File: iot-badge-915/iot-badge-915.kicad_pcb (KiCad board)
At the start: 2 copper layers, 70 x 100 mm, 68 parts, among them J1 USB_C_Receptacle_USB2.0, J2 Wire ANT, J3 Conn_01x04_Male, Q1 BC847, Q2 BC847, Q3 BC847, SW1 SW_Push, SW2 SW_Push, SW3 SW_Push, SW4 SW_Push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

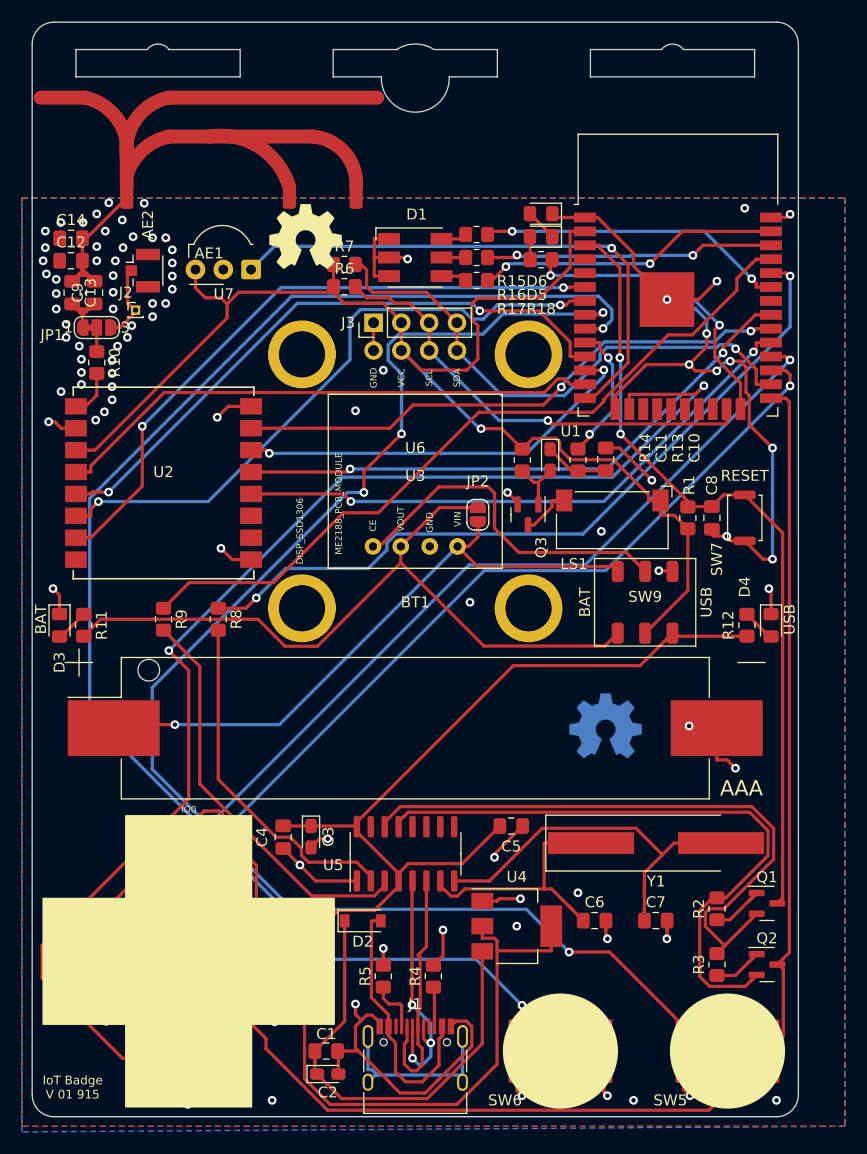
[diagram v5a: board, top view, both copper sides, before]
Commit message: added and routed audio components in 915mhz
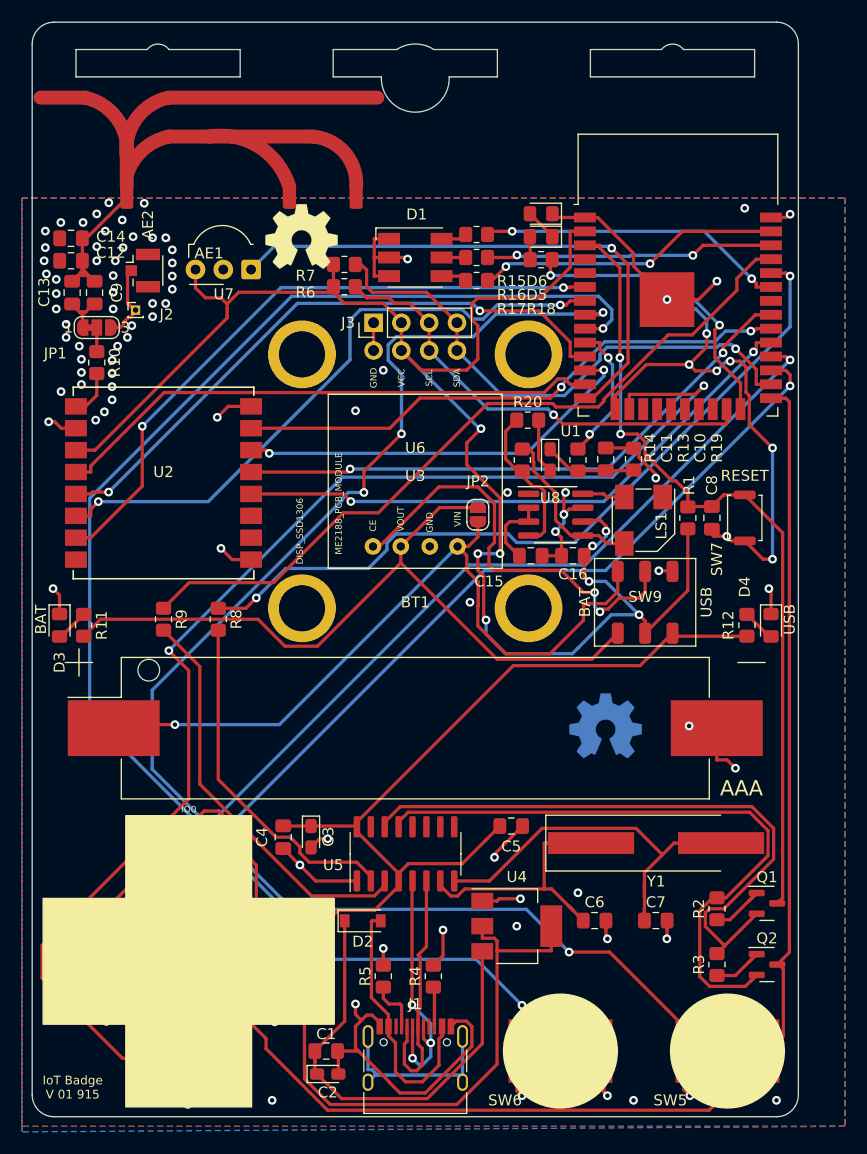
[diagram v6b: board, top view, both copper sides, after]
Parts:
- removed Q3: BC847, Package_TO_SOT_SMD:SOT-23
- added C15: 0.1uF, Capacitor_SMD:C_0805_2012Metric_Pad1.18x1.45mm_HandSolder, F.Cu at (145.6, 98.8)
- added C16: 0.1uF, Capacitor_SMD:C_0805_2012Metric_Pad1.18x1.45mm_HandSolder, F.Cu at (149.4, 98.8)
- added R19: 320, Resistor_SMD:R_0805_2012Metric_Pad1.20x1.40mm_HandSolder, F.Cu at (154.9, 89.9)
- added R20: 20k, Resistor_SMD:R_0805_2012Metric_Pad1.20x1.40mm_HandSolder, F.Cu at (145.3, 86.4)
- added U8: SSM2211S, Package_SO:SOIC-8_3.9x4.9mm_P1.27mm, F.Cu at (147.8, 95.0)
- LS1: value Speaker -> Speaker_SMD; footprint Speaker_SMD:Speaker_SMD-10mmx5mm -> Speaker_SMD:Speaker_SMD-5020
- R13: value 220 -> 620
- R14: value 2.2k -> 20k
- moved LS1 2.85 mm to (155.8, 95.5), turned to -90 degrees
- moved SYMB2 0.37 mm to (124.6, 69.6)
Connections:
- LS1 pad 1: +3V3 -> unconnected-(LS1-Pad1)
- R14 pad 1: +3V3 -> Net-(LS1-Pad3)
- R14 pad 2: Net-(C11-Pad2) -> Net-(R20-Pad1)
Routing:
- net +3V3: track 122.9 -> 153.5 mm, vias 1 -> 8
- net Net-(LS1-Pad3): track 0.00 -> 15.5 mm
- net Net-(R20-Pad1): track 0.00 -> 14.3 mm
- net +BATT: track 57.5 -> 68.9 mm
- net Earth: track 200.6 -> 209.2 mm, vias 102 -> 104
- net Net-(SW9-Pad5): track 32.2 -> 39.2 mm, vias 0 -> 2
- net Net-(C15-Pad1): track 0.00 -> 6.81 mm
- net Net-(AE1-Pad1): track 18.1 -> 14.0 mm
- net Net-(C13-Pad2): track 7.56 -> 4.49 mm
- net Net-(C10-Pad1): track 5.91 -> 8.47 mm
- net /EN: track 73.7 -> 74.8 mm
- net Net-(JP2-Pad2): track 67.3 -> 68.3 mm
- net Net-(R8-Pad1): track 69.8 -> 70.4 mm
- net Net-(LS1-Pad2): track 4.56 -> 3.92 mm
- net /SDA: track 50.5 -> 49.9 mm

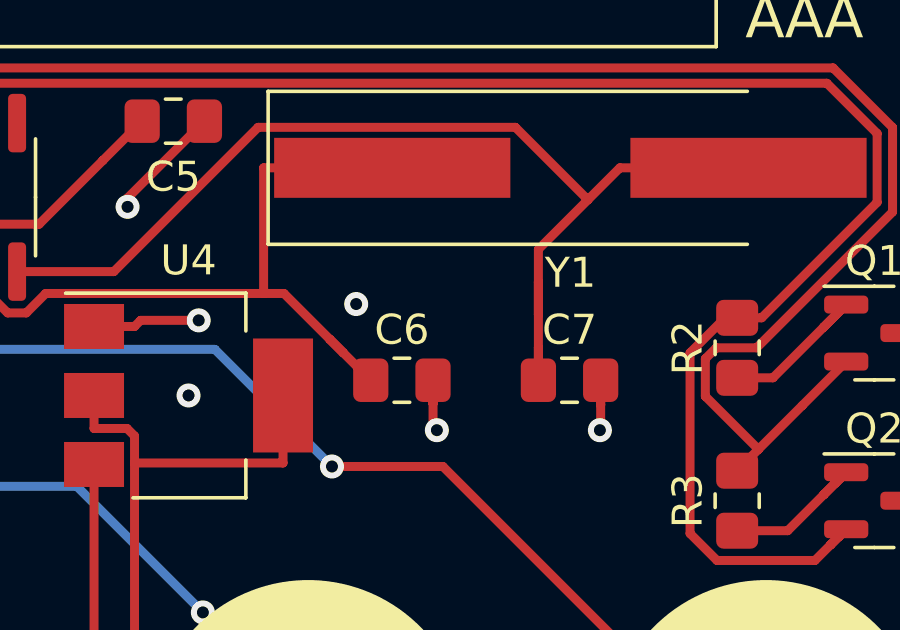
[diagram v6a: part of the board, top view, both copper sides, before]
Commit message: moved xtal capacitors to make some room
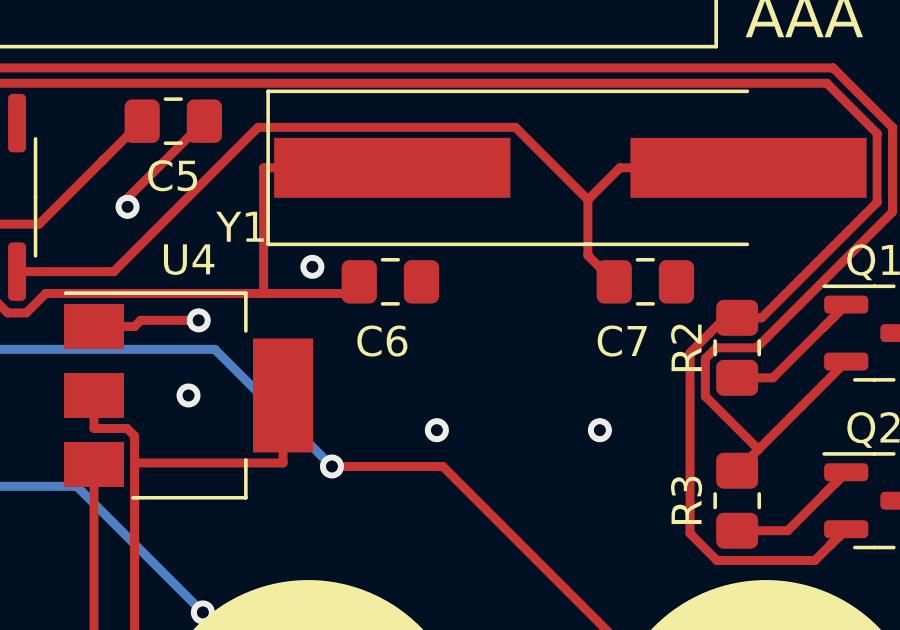
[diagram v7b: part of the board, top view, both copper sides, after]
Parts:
- moved C7 4.14 mm to (159.5, 128.8)
- moved C6 3.30 mm to (151.0, 128.8)
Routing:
- net Net-(C7-Pad1): track 36.7 -> 30.9 mm
- net Earth: track 209.2 -> 204.2 mm
- net Net-(C6-Pad1): track 25.1 -> 22.4 mm

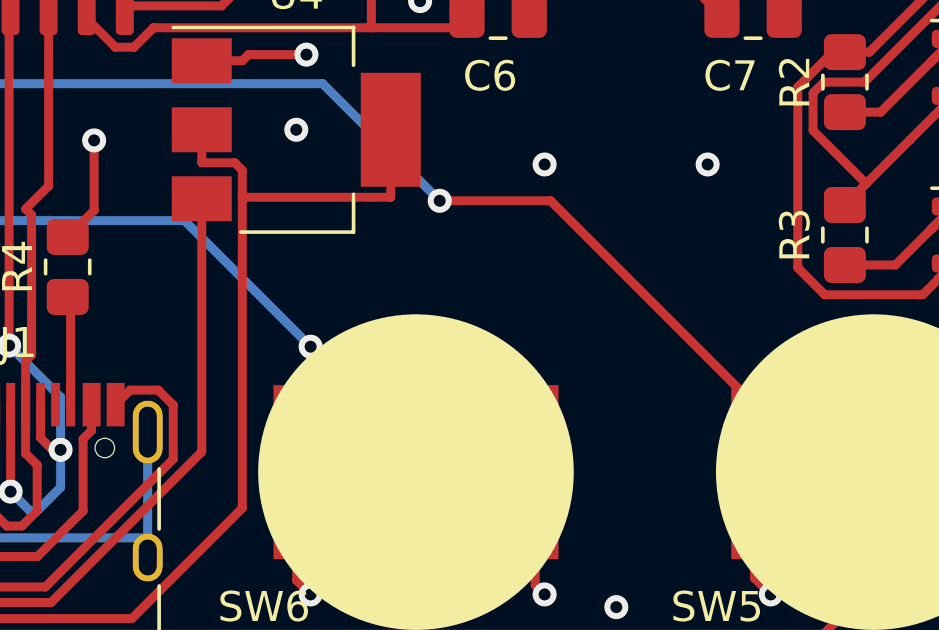
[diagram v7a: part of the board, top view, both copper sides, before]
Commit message: added resistors to sw to protect against shorts
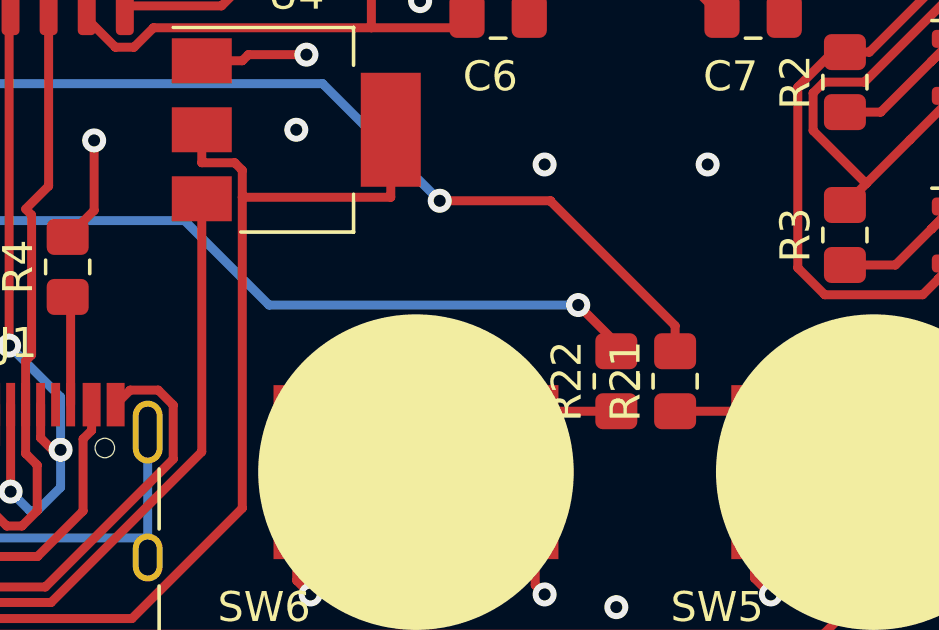
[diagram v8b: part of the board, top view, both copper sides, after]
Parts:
- added R21: 220, Resistor_SMD:R_0805_2012Metric_Pad1.20x1.40mm_HandSolder, F.Cu at (156.9, 141.0)
- added R22: 220, Resistor_SMD:R_0805_2012Metric_Pad1.20x1.40mm_HandSolder, F.Cu at (154.9, 141.0)
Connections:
- SW5 pad 1: /SW5-32 -> Net-(SW5-Pad1)
- SW6 pad 1: /SW6-33 -> Net-(SW6-Pad1)
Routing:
- net Net-(SW6-Pad1): track 0.00 -> 11.4 mm
- net /SW5-32: track 138.4 -> 127.6 mm
- net Net-(SW5-Pad1): track 0.00 -> 10.7 mm
